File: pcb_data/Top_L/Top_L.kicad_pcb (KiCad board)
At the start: 2 copper layers, 158.4 x 96.4 mm, 85 parts, among them J1 Conn_01x02, U1 XIAO-nRF52840

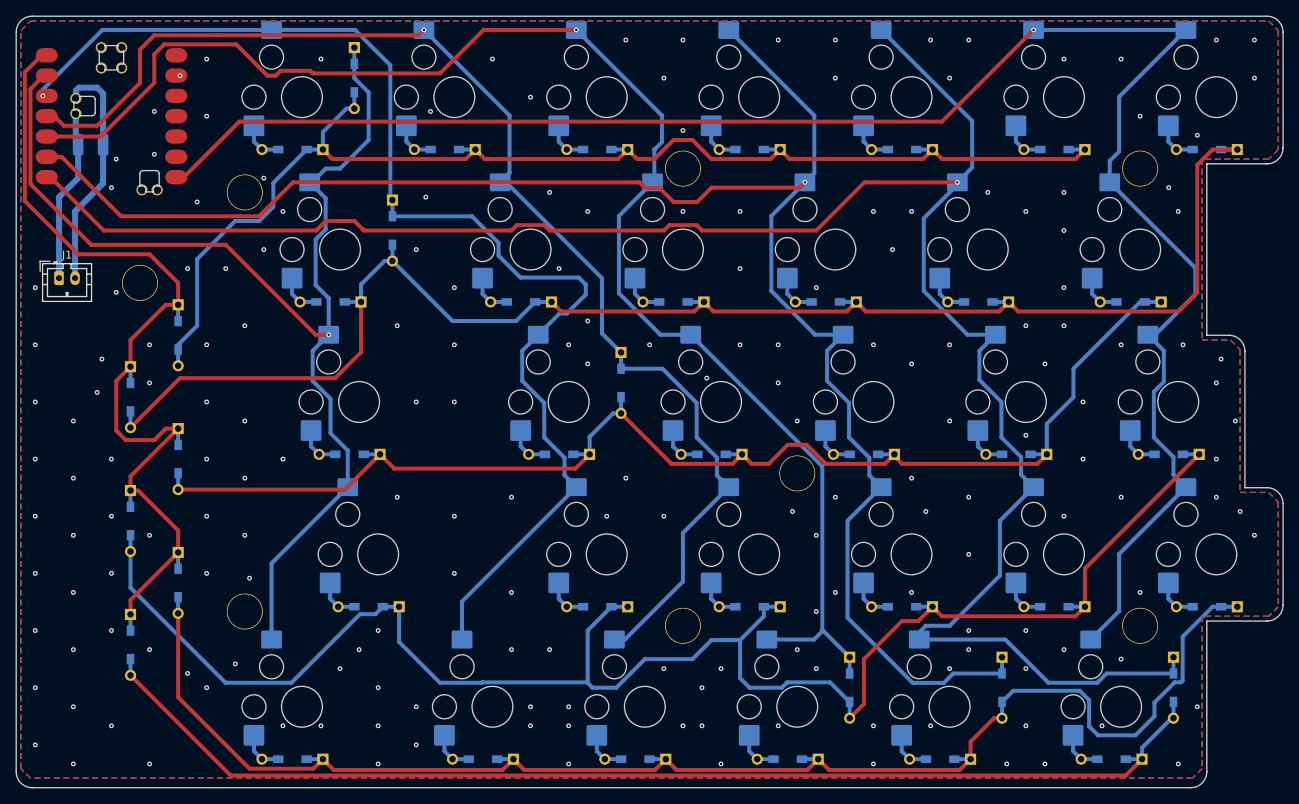
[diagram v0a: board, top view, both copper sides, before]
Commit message: remove segment and via
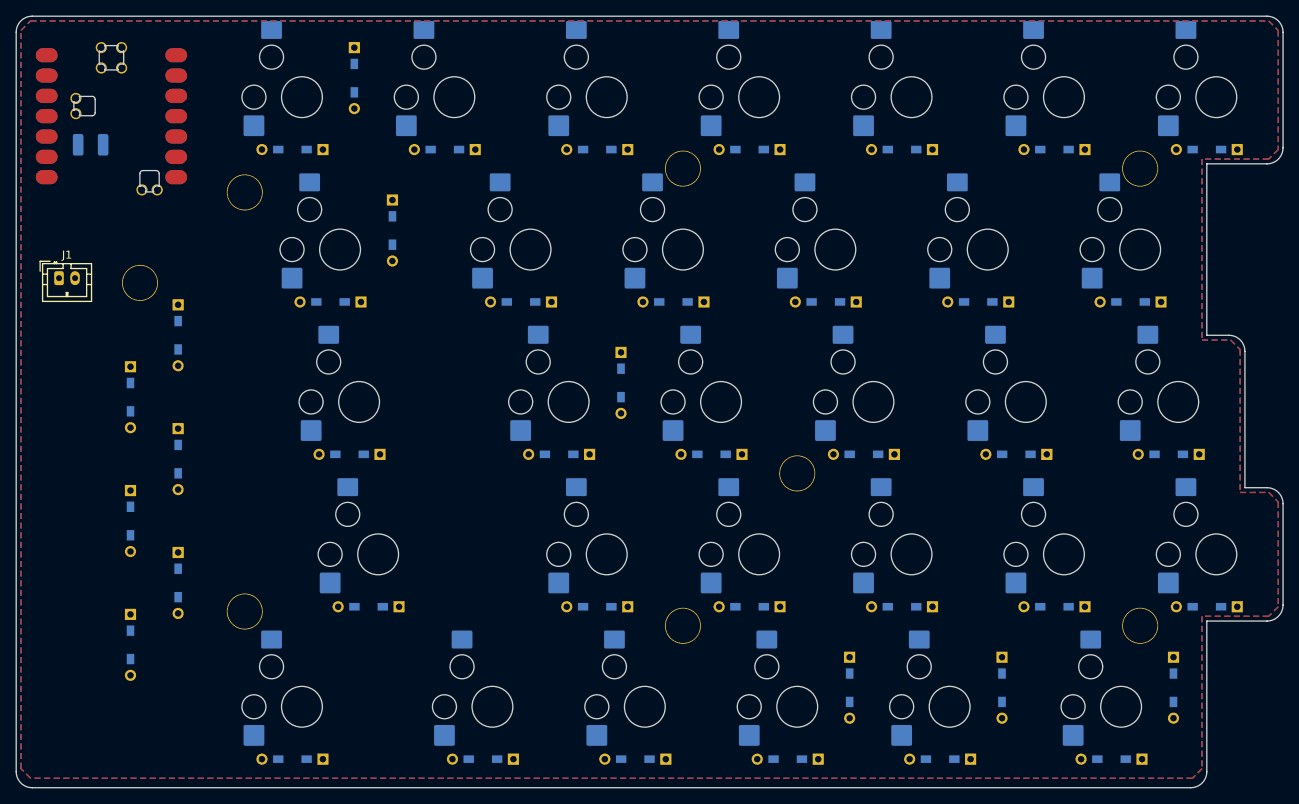
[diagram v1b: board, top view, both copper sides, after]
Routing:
- net IO 5: track 257.7 -> 0.00 mm, vias 1 -> 0
- net IO 6: track 229.0 -> 0.00 mm, vias 1 -> 0
- net IO 4: track 217.6 -> 0.00 mm, vias 1 -> 0
- net Net-(D0-3-K): track 214.1 -> 0.00 mm
- net Net-(D0-1-K): track 191.5 -> 0.00 mm
- net IO 3: track 186.5 -> 0.00 mm, vias 1 -> 0
- net Net-(D0-4-K): track 185.1 -> 0.00 mm
- net Net-(D0-2-K): track 163.2 -> 0.00 mm
- net IO 2: track 159.4 -> 0.00 mm, vias 1 -> 0
- net Net-(D1-0-K): track 159.2 -> 0.00 mm
- net IO 1: track 153.7 -> 0.00 mm, vias 1 -> 0
- net IO 0: track 147.0 -> 0.00 mm, vias 1 -> 0
- net Net-(D6-5-K): track 145.5 -> 0.00 mm
- net INTR_L: track 118.4 -> 0.00 mm
- net GND: track 29.4 -> 0.00 mm, vias 192 -> 0
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
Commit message: remove zone
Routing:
- removed copper zone on B.Cu, net GND
- removed copper zone on F.Cu, net GND
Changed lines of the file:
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@@
 		(layer "Edge.Cuts")
-	)
-	(zone
-		(net 46)
-		(net_name "GND")
-		(layers "F.Cu" "B.Cu")
-		(hatch edge 0.5)
-		(connect_pads
-			(clearance 0.5)
-		)
-		(min_thickness 0.25)
-		(filled_areas_thickness no)
-		(fill yes
-			(thermal_gap 0.5)
-			(thermal_bridge_width 0.5)
-		)
-		(polygon
-			(pts
-				(xy 201.811107 47.62504) (xy 203.001733 48.815666) (xy 203.001733 63.698491) (xy 201.811107 64.889117)
-				(xy 193.476725 64.889117) (xy 193.476725 87.511011) (xy 197.048603 87.511011) (xy 198.239229 88.701637)
-				(xy 198.239229 106.561027) (xy 201.811107 106.561027) (xy 203.001733 107.751653) (xy 203.001733 120.848539)
-				(xy 201.811107 122.039165) (xy 193.476725 122.039165) (xy 193.476725 141.089181) (xy 192.286099 142.279807)
-				(xy 47.029727 142.279807) (xy 45.839101 141.089181) (xy 45.839101 48.815666) (xy 47.029727 47.62504)
-			)
-		)
 	)
 	(embedded_fonts no)

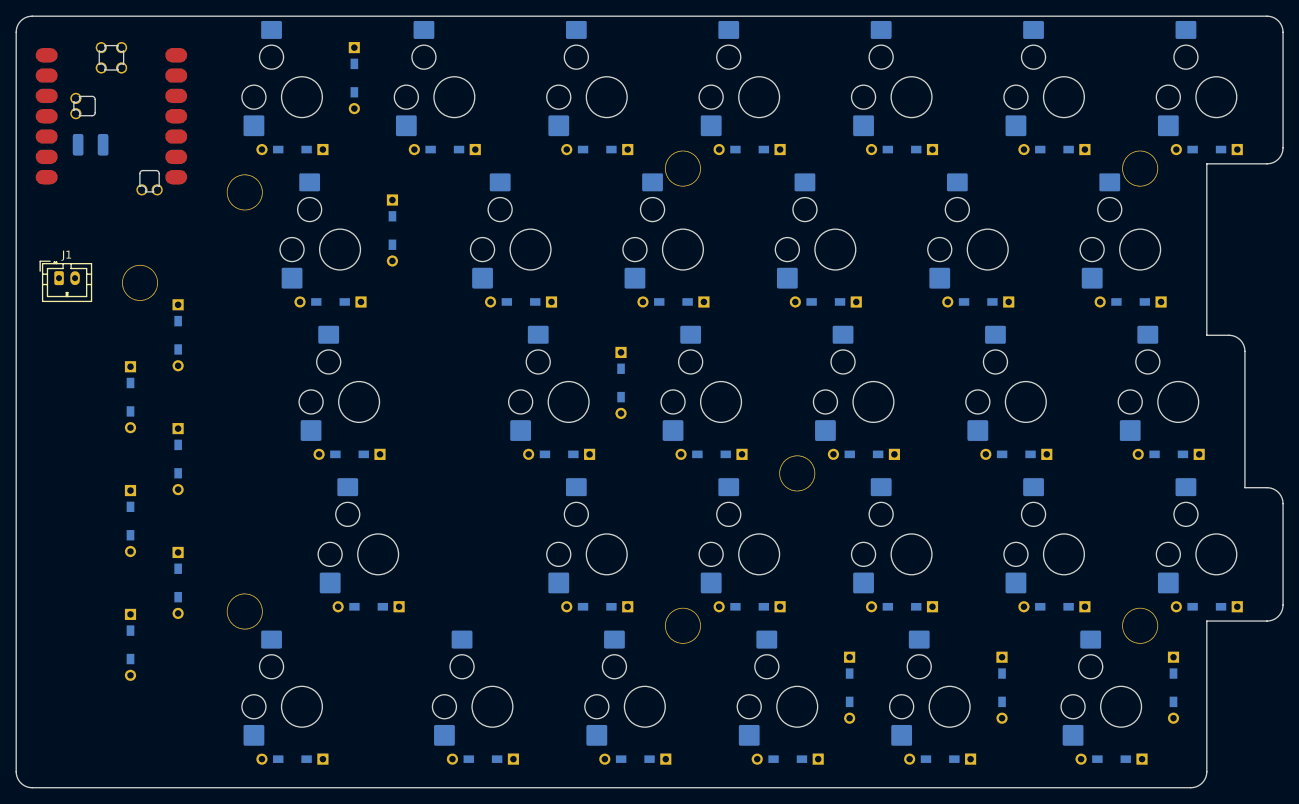
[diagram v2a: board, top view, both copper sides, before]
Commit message: remove diode
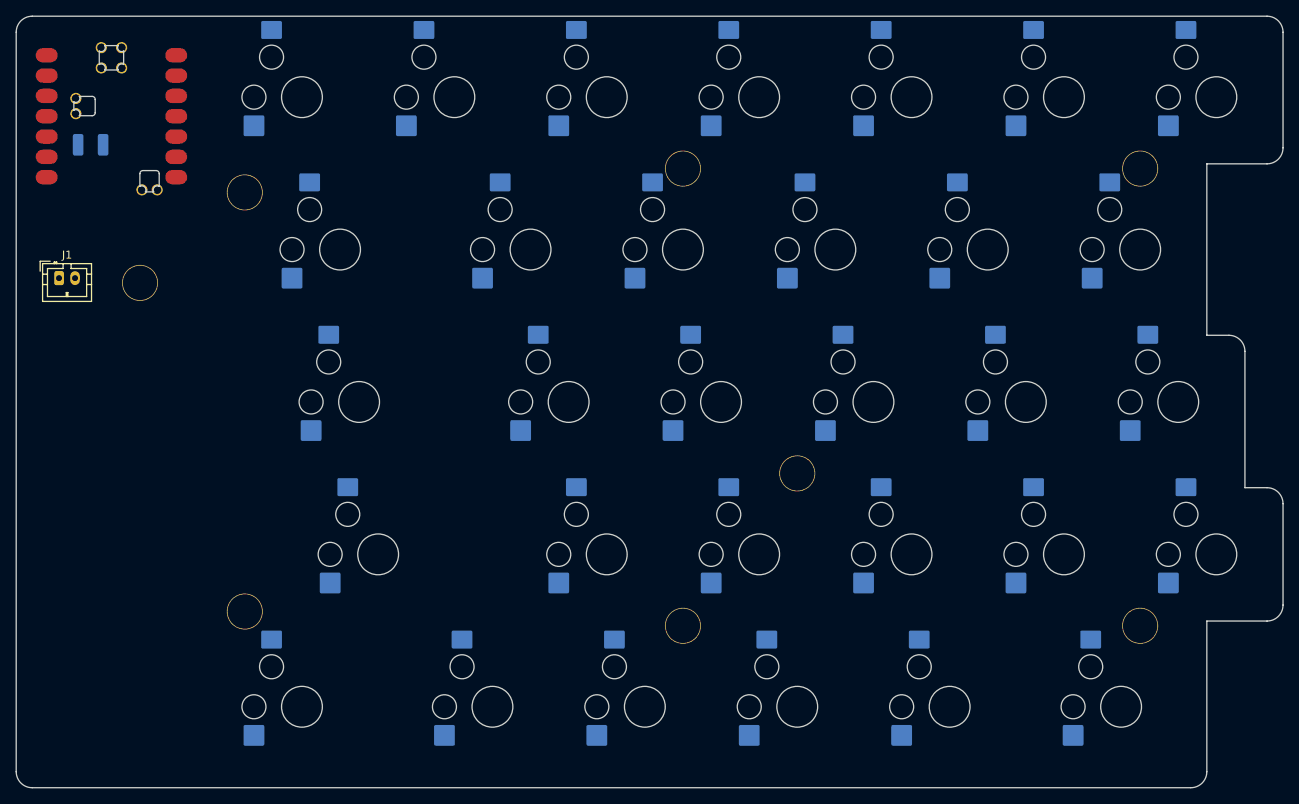
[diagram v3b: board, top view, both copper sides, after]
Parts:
- removed D0-1, D0-2, D0-3, D0-4, D1-0, D1-2, D1-3, D1-4, D2-0, D2-1, D2-3, D2-4, D3-0, D3-1, D3-2, D3-4, D4-0, D4-1, D4-2, D4-3, D5-0, D5-1, D5-2, D5-3, D5-4, D6-0, D6-1, D6-2, D6-3, D6-4, D6-5, DI0, DI1, DI2, DI3, DI4, DI5, DS0, DS1, DS2, DS3, DS4, DS5: 1N4148W, kbd_Parts:Diode_TH_SMD

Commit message: replace switch footprint
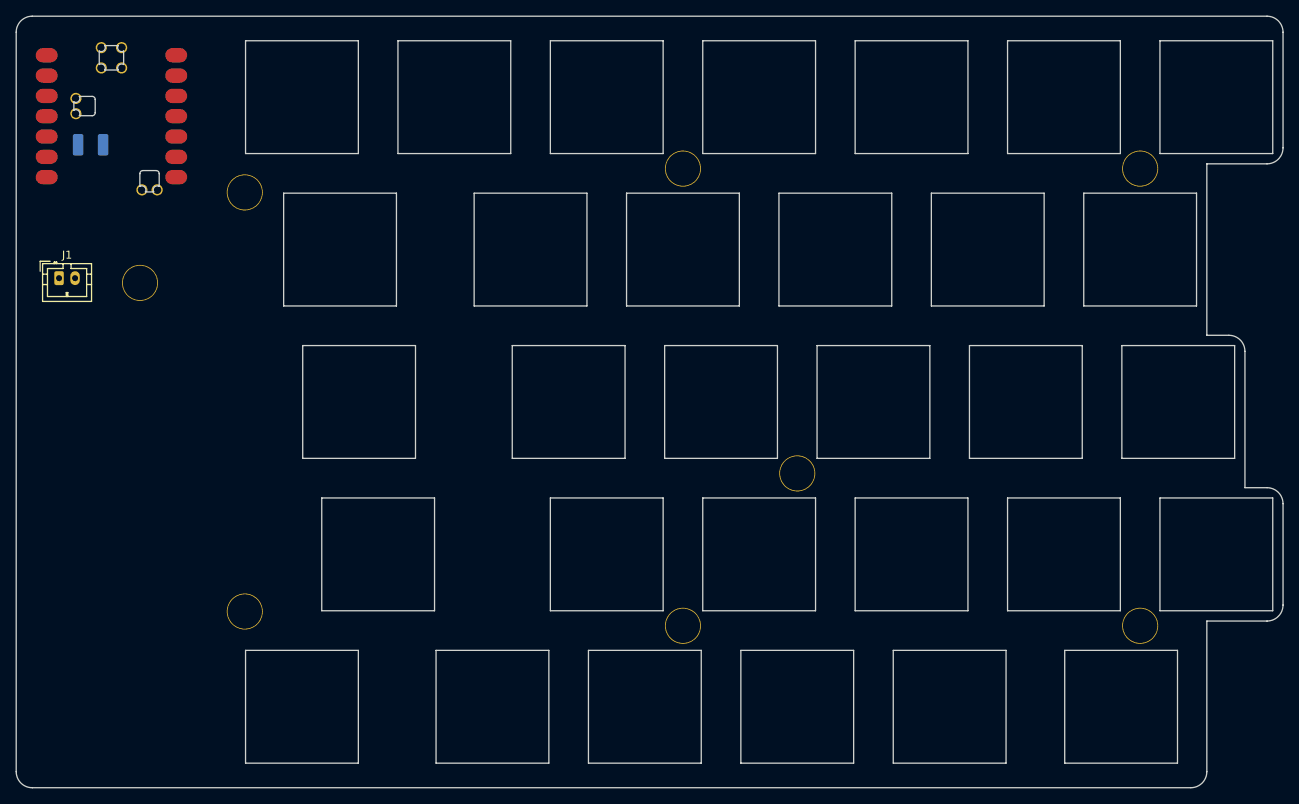
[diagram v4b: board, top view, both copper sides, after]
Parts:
- RC0-1: footprint custom-library:Kailh-PG1353-Hotswap-L-1.5U -> kbd_SW_Hole:SW_Hole_1.5u
- RC0-2: footprint custom-library:Kailh-PG1353-Hotswap-L-1.75U -> kbd_SW_Hole:SW_Hole_1.75u
- RC0-3: footprint custom-library:Kailh-PG1353-Hotswap-L-2U -> custom-library:SW_Hole_2u
- RC0-4, RC1-0, RC1-2, RC1-3, RC1-4, RC2-0, RC2-1, RC2-3, RC2-4, RC3-0, RC3-1, RC3-2, RC3-4, RC4-0, RC4-1, RC4-2, RC4-3, RC5-0, RC5-1, RC5-2, RC5-3, RC5-4, RC6-0, RC6-1, RC6-2, RC6-3, RC6-4: footprint custom-library:Kailh-PG1353-Hotswap-L-1U -> kbd_SW_Hole:SW_Hole_1u
- RC6-5: footprint custom-library:Kailh-PG1353-Hotswap-L-1.25U -> kbd_SW_Hole:SW_Hole_1.25u

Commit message: update line
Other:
- board size 158.4 x 96.4 mm -> 134.5 x 96.4 mm
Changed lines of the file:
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@@
 	)
 	(gr_arc
-		(start 47.243787 143.470433)
-		(mid 45.829574 142.884647)
-		(end 45.243787 141.470434)
+		(start 71.05625 143.470433)
+		(mid 69.642036 142.884647)
+		(end 69.05625 141.470434)
 		(stroke
 			(width 0.05)
@@
 	(gr_line
 		(start 201.597046 47.029727)
-		(end 47.24375 47.029727)
+		(end 71.05625 47.029727)
 		(stroke
 			(width 0.05)
@@
 	)
 	(gr_arc
-		(start 45.24375 49.029727)
-		(mid 45.82953 47.615514)
-		(end 47.24375 47.029727)
+		(start 69.05625 49.029727)
+		(mid 69.642036 47.615513)
+		(end 71.05625 47.029727)
 		(stroke
 			(width 0.05)
@@
 	)
 	(gr_line
-		(start 47.243787 143.470433)
+		(start 71.05625 143.470433)
 		(end 192.072038 143.470433)
 		(stroke
@@
 	)
 	(gr_line
-		(start 45.24375 49.029727)
-		(end 45.243787 141.470434)
+		(start 69.05625 49.029727)
+		(end 69.05625 141.470434)
 		(stroke
 			(width 0.05)
